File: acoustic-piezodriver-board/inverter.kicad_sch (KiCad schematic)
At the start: 32 parts, among them P201 WJ128V-5.0-3P, U201 UCC27282DR, U202 UCC27282DR, U204 TMCS1108A3UQDR, U6 NCE6005AS, U7 NCE6005AS

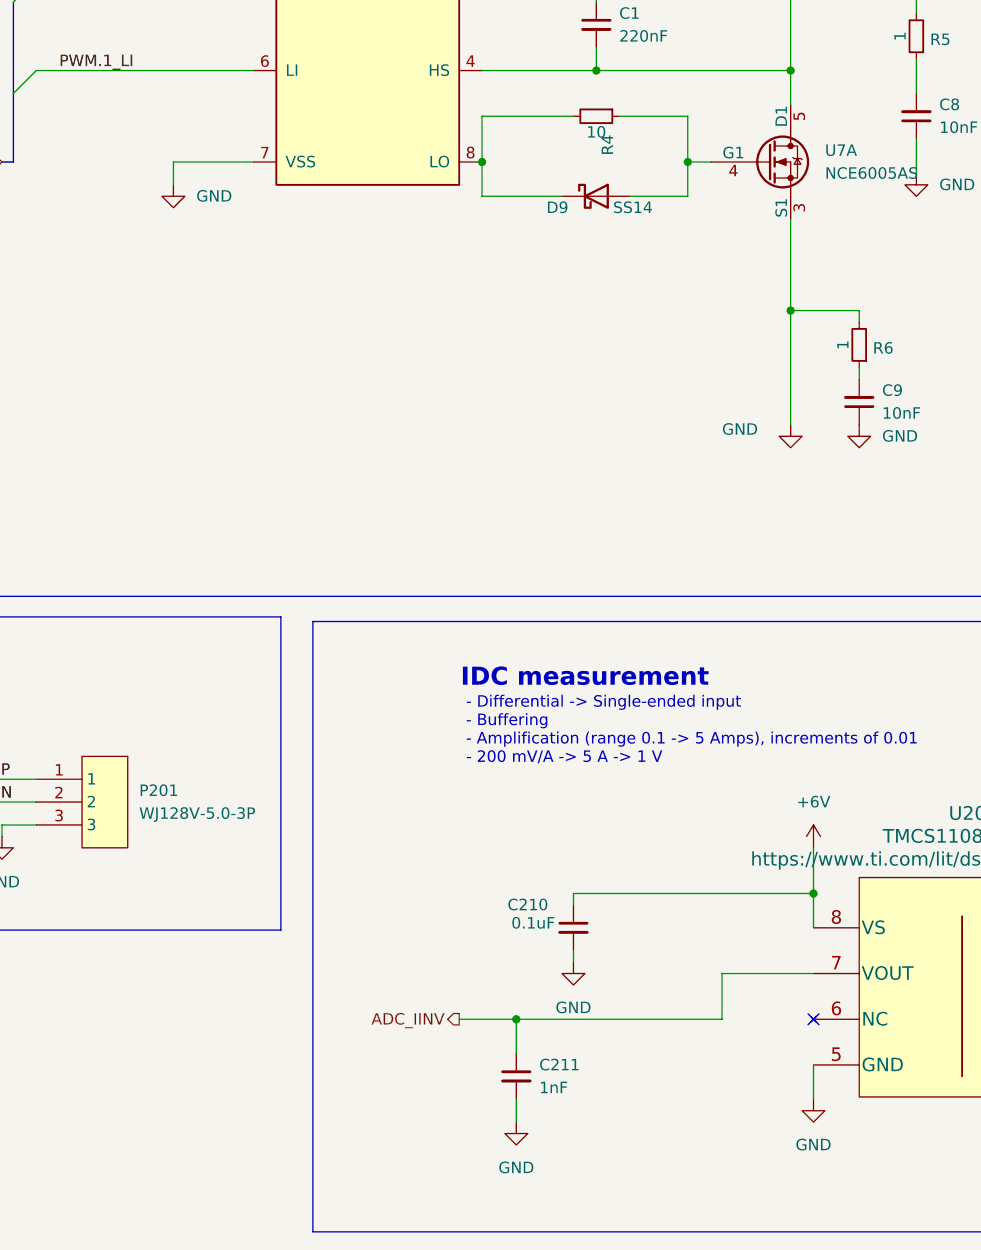
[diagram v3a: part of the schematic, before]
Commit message: replaced dual 10uH inductors with single 22uH higher VDC resistant one, started laying out 40 V boost
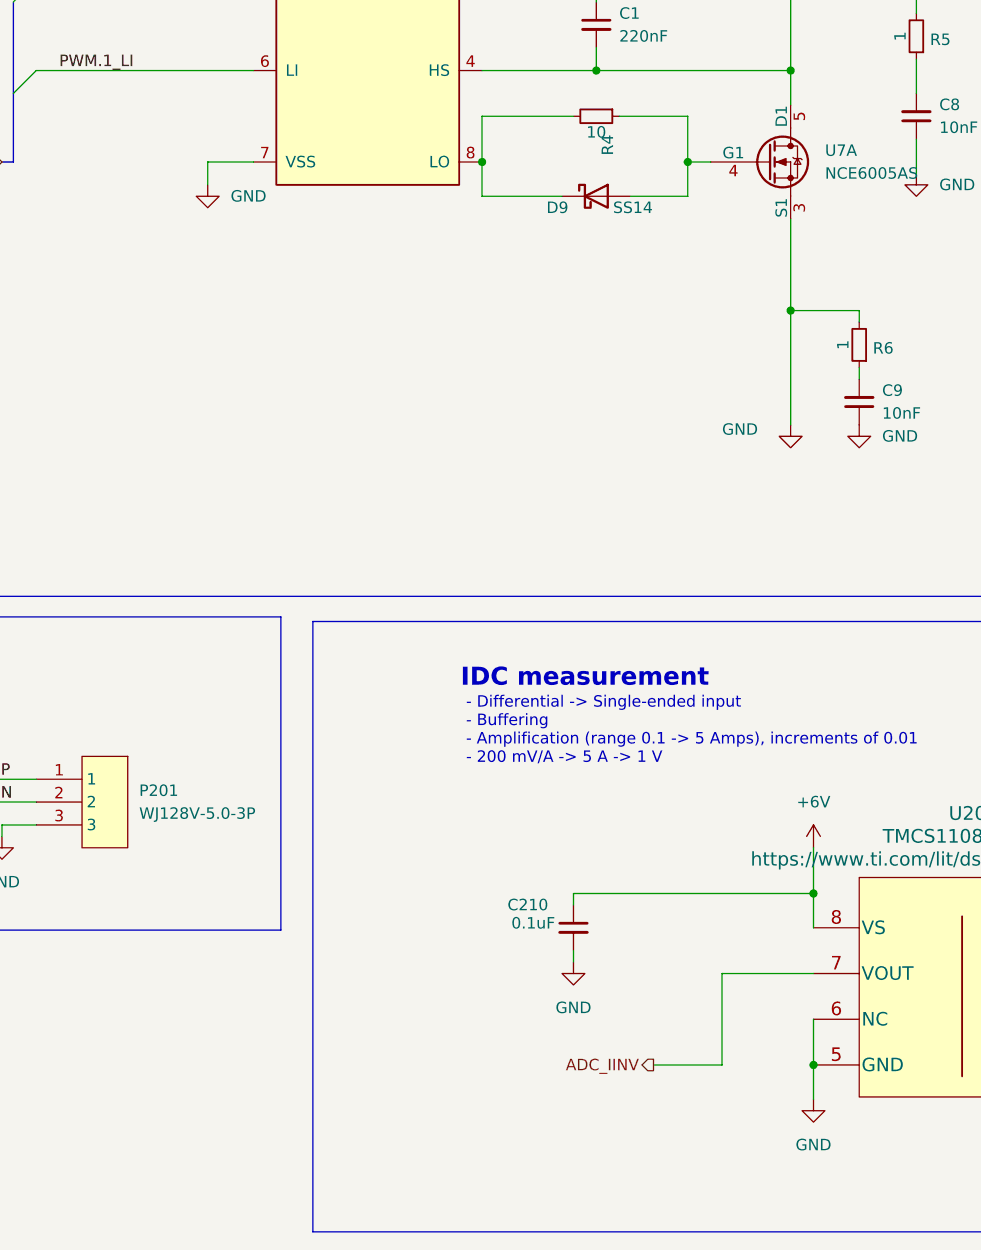
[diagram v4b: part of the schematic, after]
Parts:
- removed C211: 1nF, Capacitor_SMD:C_0402_1005Metric, symbol Device:C_Small
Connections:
- net GND: now also U201.9 (VSS), U202.9 (VSS), U204.6 (NC)
- no-connect marks 1 -> 0
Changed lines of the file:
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@@
 	)
 	(junction
-		(at 91.44 203.2)
-		(diameter 0)
-		(color 0 0 0 0)
-	)
-	(junction
 		(at 243.84 110.49)
 		(diameter 0)
@@
 	)
 	(junction
+		(at 124.46 208.28)
+		(diameter 0)
+		(color 0 0 0 0)
+	)
+	(junction
 		(at 121.92 97.79)
 		(diameter 0)
@@
 		(color 0 0 0 0)
 	)
-	(no_connect
-		(at 124.46 203.2)
-	)
 	(bus_entry
 		(at 38.1 87.63)
@@
 	(wire
 		(pts
-			(xy 91.44 214.63) (xy 91.44 212.09)
-		)
-		(stroke
-			(width 0)
-			(type default)
-		)
-	)
-	(wire
-		(pts
 			(xy 113.03 41.91) (xy 128.27 41.91)
 		)
@@
 	(wire
 		(pts
-			(xy 62.23 107.95) (xy 53.34 107.95)
+			(xy 62.23 107.95) (xy 57.15 107.95)
 		)
 		(stroke
@@
 	(wire
 		(pts
-			(xy 91.44 207.01) (xy 91.44 203.2)
+			(xy 252.73 100.33) (xy 252.73 104.14)
 		)
 		(stroke
@@
 	(wire
 		(pts
-			(xy 252.73 100.33) (xy 252.73 104.14)
+			(xy 237.49 99.06) (xy 237.49 100.33)
 		)
 		(stroke
@@
 	(wire
 		(pts
-			(xy 237.49 99.06) (xy 237.49 100.33)
+			(xy 25.4 176.53) (xy 38.1 176.53)
 		)
 		(stroke
@@
 	(wire
 		(pts
-			(xy 25.4 176.53) (xy 38.1 176.53)
+			(xy 252.73 96.52) (xy 252.73 100.33)
 		)
 		(stroke
@@
 	(wire
 		(pts
-			(xy 252.73 96.52) (xy 252.73 100.33)
+			(xy 107.95 80.01) (xy 107.95 81.28)
 		)
 		(stroke
@@
 	(wire
 		(pts
-			(xy 107.95 80.01) (xy 107.95 81.28)
+			(xy 257.81 41.91) (xy 257.81 57.15)
 		)
 		(stroke
@@
 	(wire
 		(pts
-			(xy 257.81 41.91) (xy 257.81 57.15)
+			(xy 124.46 203.2) (xy 124.46 208.28)
 		)
 		(stroke
@@
 	(wire
 		(pts
-			(xy 53.34 107.95) (xy 53.34 110.49)
+			(xy 57.15 107.95) (xy 57.15 110.49)
 		)
 		(stroke
@@
 	(wire
 		(pts
-			(xy 114.3 203.2) (xy 114.3 198.12)
+			(xy 114.3 208.28) (xy 114.3 198.12)
 		)
 		(stroke
@@
 	(wire
 		(pts
-			(xy 91.44 203.2) (xy 114.3 203.2)
-		)
-		(stroke
-			(width 0)
-			(type default)
-		)
-	)
-	(wire
-		(pts
 			(xy 107.95 81.28) (xy 107.95 86.36)
 		)
@@
 	(wire
 		(pts
-			(xy 85.09 203.2) (xy 91.44 203.2)
+			(xy 106.68 208.28) (xy 114.3 208.28)
 		)
 		(stroke
@@
 	(hierarchical_label "ADC_IINV"
 		(shape output)
-		(at 85.09 203.2 180)
+		(at 106.68 208.28 180)
 		(effects
 			(font
@@
 	)
 	(symbol
-		(lib_id "Device:C_Small")
-		(at 91.44 209.55 0)
-		(unit 1)
-		(exclude_from_sim no)
-		(in_bom yes)
-		(on_board yes)
-		(dnp no)
-		(fields_autoplaced yes)
-		(property "Reference" "C211"
-			(at 93.98 208.2862 0)
-			(effects
-				(font
-					(size 1.27 1.27)
-				)
-				(justify left)
-			)
-		)
-		(property "Value" "1nF"
-			(at 93.98 210.8262 0)
-			(effects
-				(font
-					(size 1.27 1.27)
-				)
-				(justify left)
-			)
-		)
-		(property "Footprint" "Capacitor_SMD:C_0402_1005Metric"
-			(at 91.44 209.55 0)
-			(effects
-				(font
-					(size 1.27 1.27)
-				)
-				(hide yes)
-			)
-		)
-		(property "Datasheet" "https://jlcpcb.com/api/file/downloadByFileSystemAccessId/8579707266641018880"
-			(at 91.44 209.55 0)
-			(effects
-				(font
-					(size 1.27 1.27)
-				)
-				(hide yes)
-			)
-		)
-		(property "Description" "Unpolarized capacitor, small symbol"
-			(at 91.44 209.55 0)
-			(effects
-				(font
-					(size 1.27 1.27)
-				)
-				(hide yes)
-			)
-		)
-		(property "LPN" "C1523"
-			(at 91.44 209.55 0)
-			(effects
-				(font
-					(size 1.27 1.27)
-				)
-				(hide yes)
-			)
-		)
-		(property "MPN" "0402B102K500NT"
-			(at 91.44 209.55 0)
-			(effects
-				(font
-					(size 1.27 1.27)
-				)
-				(hide yes)
-			)
-		)
-		(pin "1"
-		)
-		(pin "2"
-		)
-		(instances
-			(project "acoustic-piezodriver-board"
-				(path "/94cb090f-214e-44cc-b8ed-ae50ff29d2bf/0f73f174-3d76-44ea-b4fb-f42a113ccf94"
-					(reference "C211")
-					(unit 1)
-				)
-			)
-		)
-	)
-	(symbol
 		(lib_id "iw-power:UCC27282DR")
 		(at 74.93 92.71 0)
@@
 		(pin "1"
 		)
+		(pin "9"
+		)
 		(instances
 			(project "acoustic-piezodriver-board"
@@
 	(symbol
 		(lib_id "power:GND")
-		(at 91.44 214.63 0)
-		(unit 1)
-		(exclude_from_sim no)
-		(in_bom yes)
-		(on_board yes)
-		(dnp no)
-		(fields_autoplaced yes)
-		(property "Reference" "#PWR0207"
-			(at 91.44 220.98 0)
-			(effects
-				(font
-					(size 1.27 1.27)
-				)
-				(hide yes)
-			)
-		)
-		(property "Value" "GND"
-			(at 91.44 219.71 0)
-			(effects
-				(font
-					(size 1.27 1.27)
-				)
-			)
-		)
-		(property "Footprint" ""
-			(at 91.44 214.63 0)
-			(effects
-				(font
-					(size 1.27 1.27)
-				)
-				(hide yes)
-			)
-		)
-		(property "Datasheet" ""
-			(at 91.44 214.63 0)
-			(effects
-				(font
-					(size 1.27 1.27)
-				)
-				(hide yes)
-			)
-		)
-		(property "Description" "Power symbol creates a global label with name \"GND\" , ground"
-			(at 91.44 214.63 0)
-			(effects
-				(font
-					(size 1.27 1.27)
-				)
-				(hide yes)
-			)
-		)
-		(pin "1"
-		)
-		(instances
-			(project "acoustic-piezodriver-board"
-				(path "/94cb090f-214e-44cc-b8ed-ae50ff29d2bf/0f73f174-3d76-44ea-b4fb-f42a113ccf94"
-					(reference "#PWR0207")
-					(unit 1)
-				)
-			)
-		)
-	)
-	(symbol
-		(lib_id "power:GND")
 		(at 97.79 196.85 0)
 		(unit 1)
@@
 	(symbol
 		(lib_id "power:GND")
-		(at 53.34 110.49 0)
+		(at 57.15 110.49 0)
 		(unit 1)
 		(exclude_from_sim no)
@@
 		(fields_autoplaced yes)
 		(property "Reference" "#PWR04"
-			(at 53.34 116.84 0)
+			(at 57.15 116.84 0)
 			(effects
 				(font
@@
 		)
 		(property "Value" "GND"
-			(at 55.88 111.7599 0)
+			(at 59.69 111.7599 0)
 			(effects
 				(font
@@
 		)
 		(property "Footprint" ""
-			(at 53.34 110.49 0)
+			(at 57.15 110.49 0)
 			(effects
 				(font
@@
 		)
 		(property "Datasheet" ""
-			(at 53.34 110.49 0)
+			(at 57.15 110.49 0)
 			(effects
 				(font
@@
 		)
 		(property "Description" "Power symbol creates a global label with name \"GND\" , ground"
-			(at 53.34 110.49 0)
+			(at 57.15 110.49 0)
 			(effects
 				(font
@@
 		(pin "1"
 		)
+		(pin "9"
+		)
 		(instances

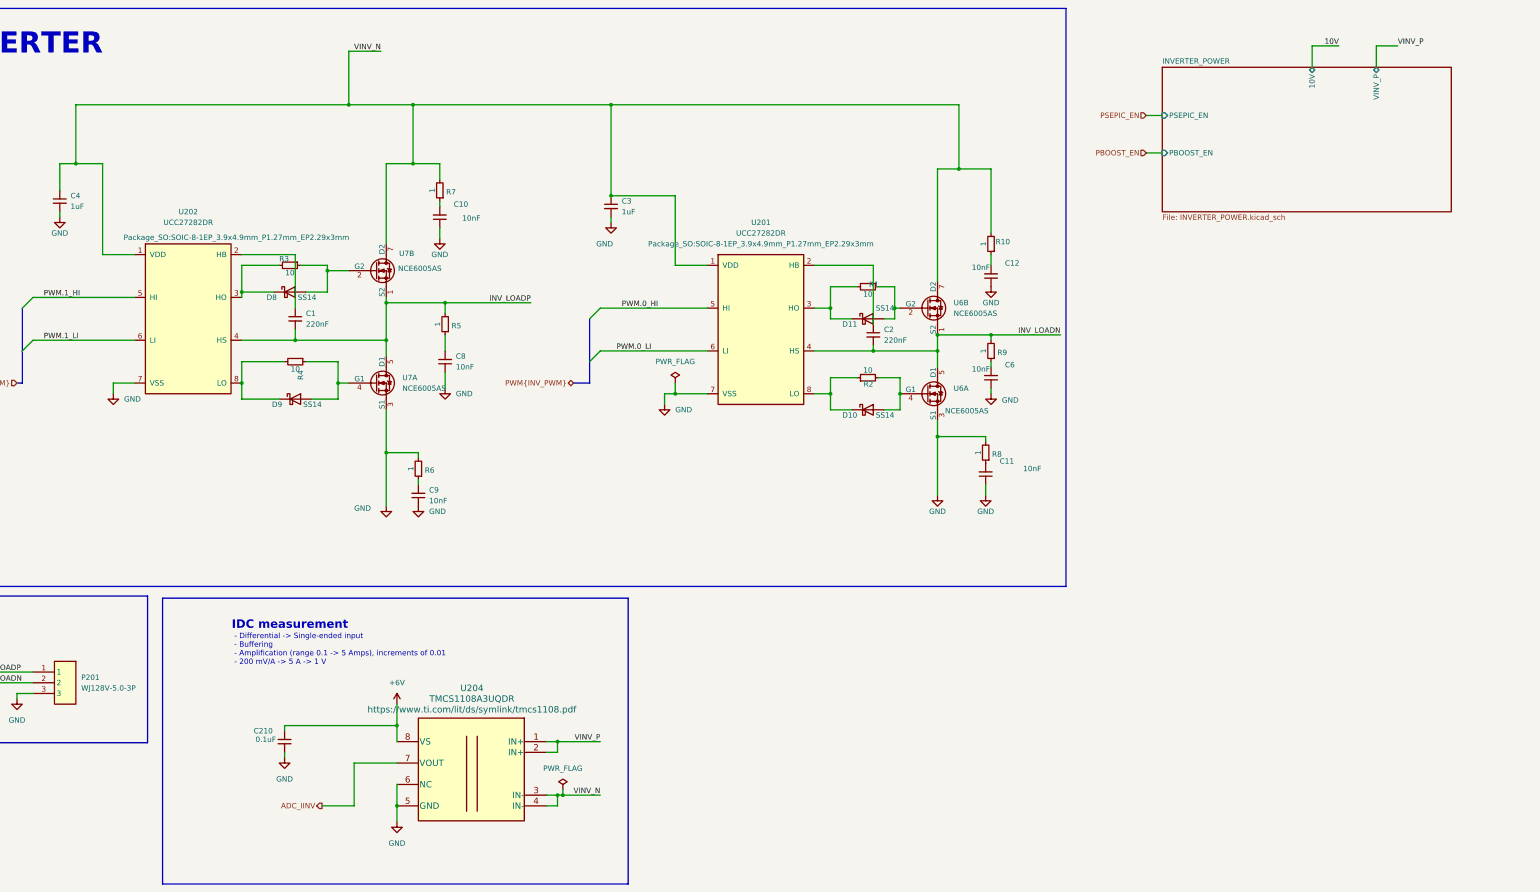
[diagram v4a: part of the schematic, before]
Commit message: placed inverter and 40 V boost (next) place 10 V SEPIC driver
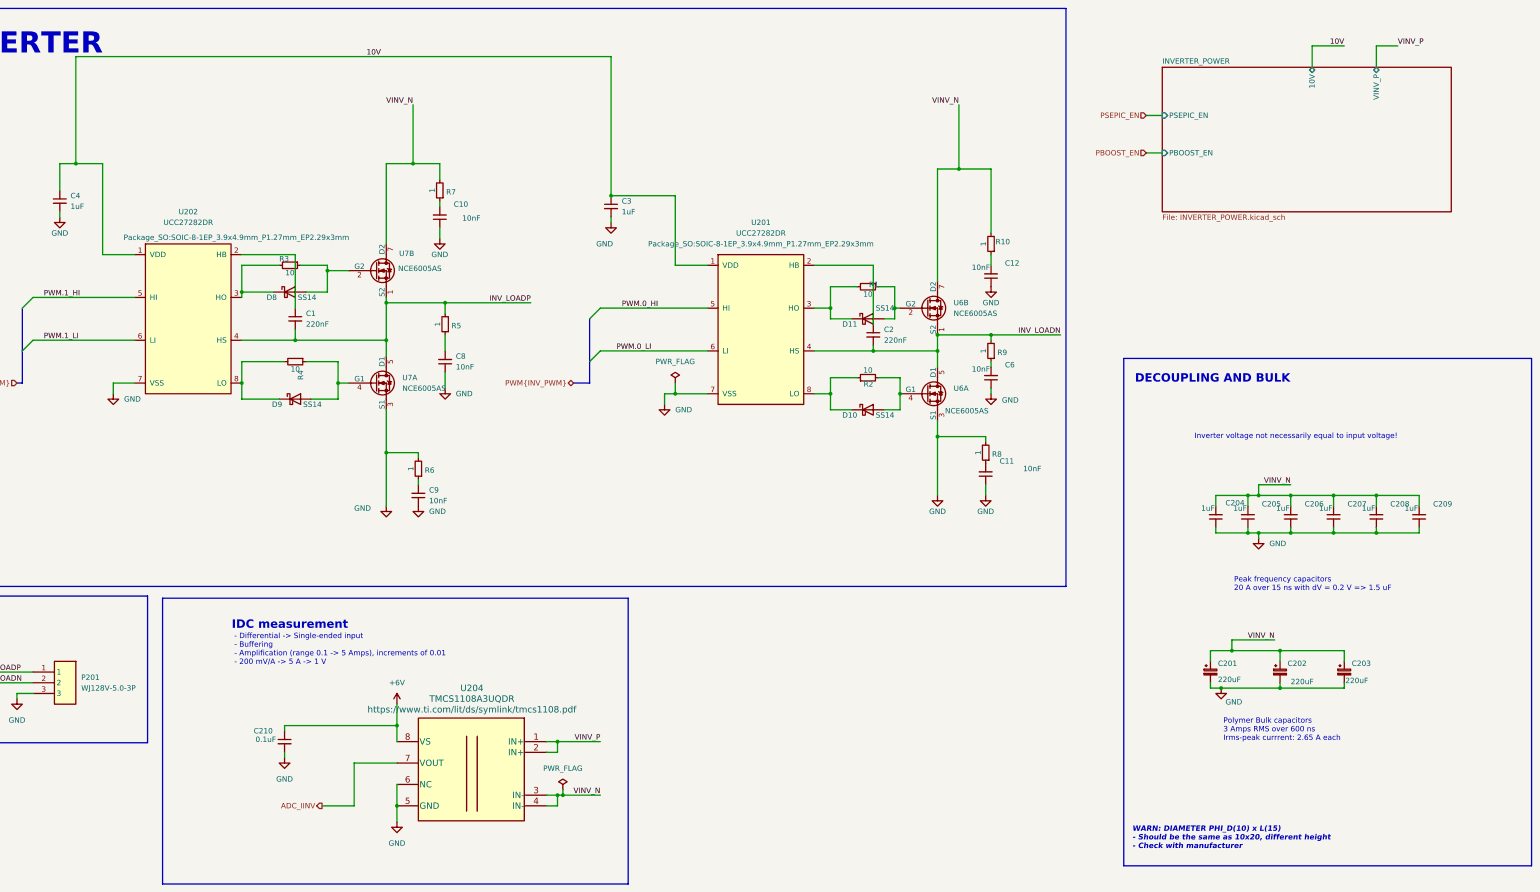
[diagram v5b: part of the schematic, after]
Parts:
- added C201, C202, C203: 220uF, Capacitor_THT:C_Radial_D10.0mm_H16.0mm_P5.00mm, symbol Device:C_Polarized_Small
- added C204, C205, C206, C207, C208, C209: 1uF, Capacitor_SMD:C_0805_2012Metric, symbol Device:C_Small
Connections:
- net 10V: now also C3.1, C4.1, U201.1 (VDD), U202.1 (VDD)
- net GND: now also C201.2, C202.2, C203.2, C204.1, C205.1, C206.1, C207.1, C208.1, C209.1
- net VINV_N: now also C201.1, C202.1, C203.1, C204.2, C205.2, C206.2, C207.2, C208.2, C209.2; no longer C3.1, C4.1, U201.1 (VDD), U202.1 (VDD)
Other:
- note added: "DECOUPLING AND BULK"
- note added: "Inverter voltage not necessarily equal to input voltage!"
- note added: "Peak frequency capacitors 20 A over 15 ns with dV = 0.2 V => 1.5 uF"
- note added: "Polymer Bulk capacitors 3 Amps RMS over 600 ns Irms-peak currrent: 2.65 A each"
- note added: "WARN: DIAMETER PHI_D(10) x L(15) - Should be the same as 10x20, different height - Check with manufacturer"

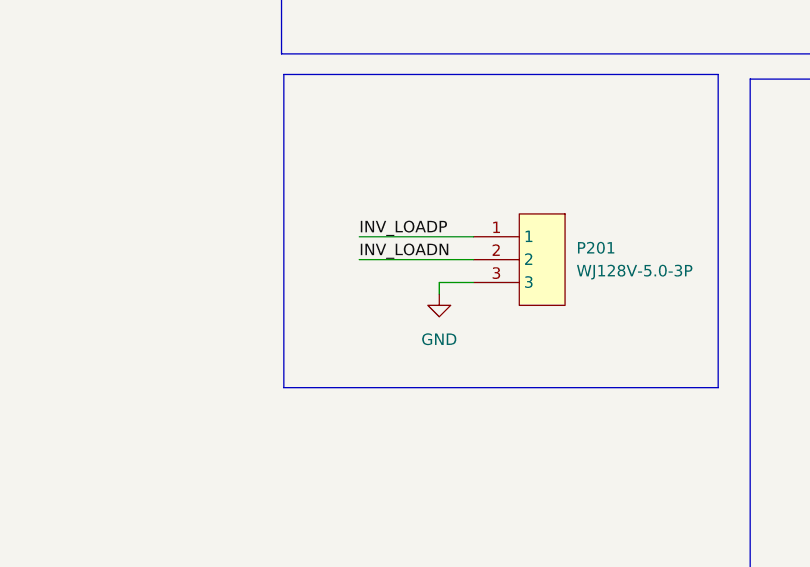
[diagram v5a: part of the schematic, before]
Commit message: completed positioning (next) routing
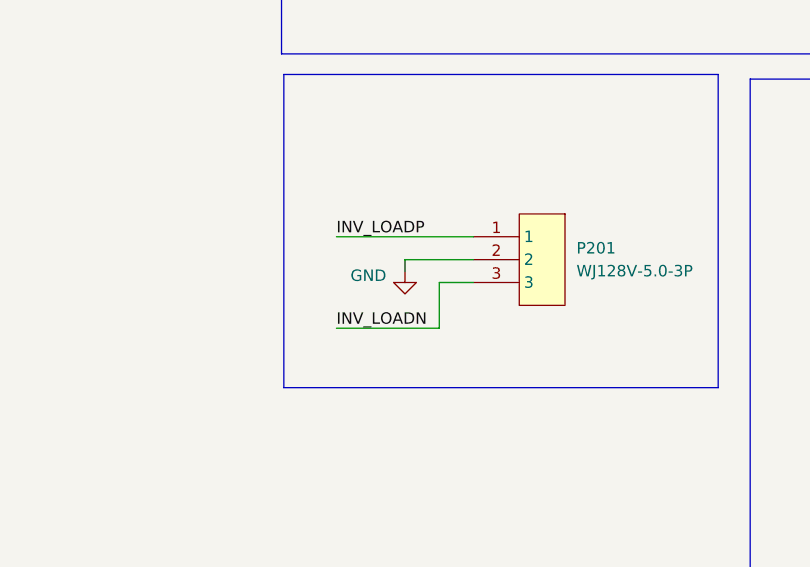
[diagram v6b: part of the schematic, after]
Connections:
- net GND: now also P201.2; no longer P201.3
- net INV_LOADN: now also P201.3; no longer P201.2
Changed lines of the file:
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@@
 	(wire
 		(pts
+			(xy 34.29 186.69) (xy 34.29 181.61)
+		)
+		(stroke
+			(width 0)
+			(type default)
+		)
+	)
+	(wire
+		(pts
 			(xy 334.01 180.34) (xy 320.04 180.34)
 		)
@@
 	(wire
 		(pts
-			(xy 25.4 176.53) (xy 38.1 176.53)
+			(xy 22.86 176.53) (xy 38.1 176.53)
 		)
 		(stroke
@@
 	(wire
 		(pts
-			(xy 25.4 179.07) (xy 38.1 179.07)
-		)
-		(stroke
-			(width 0)
-			(type default)
-		)
-	)
-	(wire
-		(pts
 			(xy 100.33 77.47) (xy 100.33 90.17)
 		)
@@
 	(wire
 		(pts
+			(xy 22.86 186.69) (xy 34.29 186.69)
+		)
+		(stroke
+			(width 0)
+			(type default)
+		)
+	)
+	(wire
+		(pts
 			(xy 44.45 55.88) (xy 44.45 62.23)
 		)
@@
 	(wire
 		(pts
+			(xy 30.48 179.07) (xy 38.1 179.07)
+		)
+		(stroke
+			(width 0)
+			(type default)
+		)
+	)
+	(wire
+		(pts
 			(xy 320.04 180.34) (xy 317.5 180.34)
 		)
@@
 	(wire
 		(pts
-			(xy 34.29 182.88) (xy 34.29 181.61)
-		)
-		(stroke
-			(width 0)
-			(type default)
-		)
-	)
-	(wire
-		(pts
 			(xy 129.54 130.81) (xy 129.54 132.08)
 		)
@@
 	(wire
 		(pts
+			(xy 30.48 180.34) (xy 30.48 179.07)
+		)
+		(stroke
+			(width 0)
+			(type default)
+		)
+	)
+	(wire
+		(pts
 			(xy 110.49 107.95) (xy 113.03 107.95)
 		)
@@
 	)
 	(label "INV_LOADN"
-		(at 25.4 179.07 0)
-		(effects
-			(font
-				(size 1.27 1.27)
-			)
-			(justify left bottom)
-		)
-	)
-	(label "INV_LOADN"
 		(at 281.94 96.52 180)
 		(effects
@@
 	)
 	(label "INV_LOADP"
-		(at 25.4 176.53 0)
+		(at 22.86 176.53 0)
 		(effects
 			(font
@@
 		)
 	)
+	(label "INV_LOADN"
+		(at 22.86 186.69 0)
+		(effects
+			(font
+				(size 1.27 1.27)
+			)
+			(justify left bottom)
+		)
+	)
 	(hierarchical_label "PWM{INV_PWM}"
 		(shape input)
@@
 	(symbol
 		(lib_id "power:GND")
-		(at 34.29 182.88 0)
+		(at 30.48 180.34 0)
 		(unit 1)
 		(exclude_from_sim no)
@@
 		(on_board yes)
 		(dnp no)
-		(fields_autoplaced yes)
 		(property "Reference" "#PWR0201"
-			(at 34.29 189.23 0)
+			(at 30.48 186.69 0)
 			(effects
 				(font
@@
 		)
 		(property "Value" "GND"
-			(at 34.29 187.96 0)
+			(at 26.416 180.848 0)
 			(effects
 				(font
@@
 		)
 		(property "Footprint" ""
-			(at 34.29 182.88 0)
+			(at 30.48 180.34 0)
 			(effects
 				(font
@@
 		)
 		(property "Datasheet" ""
-			(at 34.29 182.88 0)
+			(at 30.48 180.34 0)
 			(effects
 				(font
@@
 		)
 		(property "Description" "Power symbol creates a global label with name \"GND\" , ground"
-			(at 34.29 182.88 0)
+			(at 30.48 180.34 0)
 			(effects
 				(font
@@
 		)
 		(instances
-			(project ""
+			(project "acoustic-piezodriver-board"
 				(path "/94cb090f-214e-44cc-b8ed-ae50ff29d2bf/0f73f174-3d76-44ea-b4fb-f42a113ccf94"
 					(reference "#PWR0201")
